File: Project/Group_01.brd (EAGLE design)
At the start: 71.1 x 54.3 mm, 29 parts, among them J1 POWER_JACKPTH_LOCK, U1 +12v, U4 TMUX1208

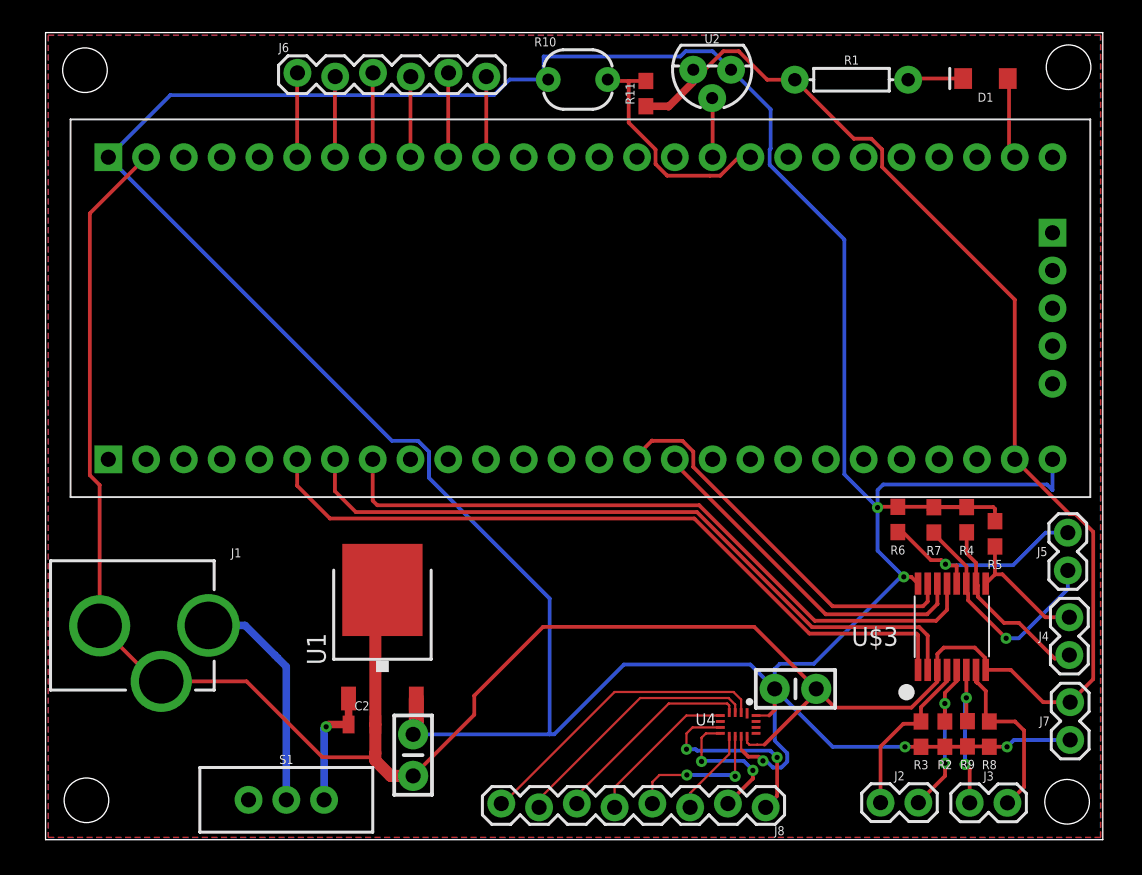
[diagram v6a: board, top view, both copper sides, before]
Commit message: Added measure in board
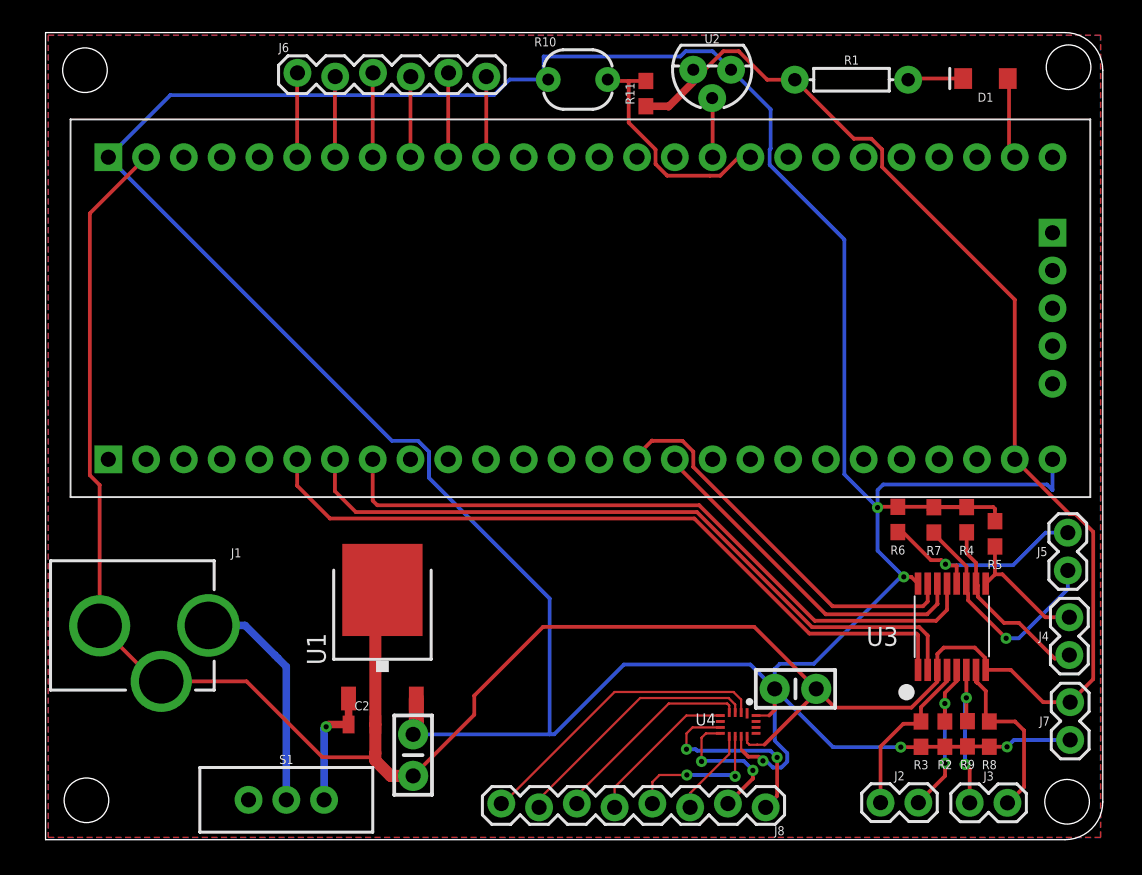
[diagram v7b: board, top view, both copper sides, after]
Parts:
- renumbered U$3 to U3
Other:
- outline, holes or cut-outs redrawn
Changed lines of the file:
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@@
 <setting verticaltext="up"/>
 </settings>
-<grid distance="0.1" unitdist="mil" unit="mil" style="lines" multiple="1" display="yes" altdistance="0.005" altunitdist="inch" altunit="inch"/>
+<grid distance="0.05" unitdist="inch" unit="inch" style="lines" multiple="1" display="yes" altdistance="0.005" altunitdist="inch" altunit="inch"/>
 <layers>
 <layer number="1" name="Top" color="4" fill="1" visible="yes" active="yes"/>
@@
 <layer number="23" name="tOrigins" color="15" fill="1" visible="yes" active="yes"/>
 <layer number="24" name="bOrigins" color="15" fill="1" visible="yes" active="yes"/>
-<layer number="25" name="tNames" color="7" fill="1" visible="yes" active="yes"/>
+<layer number="25" name="tNames" color="7" fill="1" visible="no" active="yes"/>
 <layer number="26" name="bNames" color="7" fill="1" visible="no" active="yes"/>
-<layer number="27" name="tValues" color="7" fill="1" visible="yes" active="yes"/>
+<layer number="27" name="tValues" color="7" fill="1" visible="no" active="yes"/>
 <layer number="28" name="bValues" color="7" fill="1" visible="no" active="yes"/>
 <layer number="29" name="tStop" color="7" fill="3" visible="no" active="yes"/>
 <layer number="30" name="bStop" color="7" fill="6" visible="no" active="yes"/>
-<layer number="31" name="tCream" color="7" fill="4" visible="no" active="yes"/>
+<layer number="31" name="tCream" color="7" fill="4" visible="yes" active="yes"/>
 <layer number="32" name="bCream" color="7" fill="5" visible="no" active="yes"/>
 <layer number="33" name="tFinish" color="6" fill="3" visible="no" active="yes"/>
@@
 <board>
 <plain>
-<wire x1="0" y1="0" x2="71.1" y2="0" width="0" layer="20"/>
-<wire x1="71.1" y1="0" x2="71.1" y2="54.28" width="0" layer="20"/>
-<wire x1="71.1" y1="54.28" x2="0" y2="54.28" width="0" layer="20"/>
 <wire x1="0" y1="54.28" x2="0" y2="0" width="0" layer="20"/>
+<wire x1="0" y1="0" x2="68.56" y2="0" width="0" layer="20"/>
+<wire x1="68.56" y1="0" x2="71.1" y2="2.54" width="0" layer="20" curve="90"/>
+<wire x1="71.1" y1="2.54" x2="71.1" y2="51.74" width="0" layer="20"/>
+<wire x1="71.1" y1="51.74" x2="68.56" y2="54.28" width="0" layer="20" curve="90"/>
+<wire x1="68.56" y1="54.28" x2="0" y2="54.28" width="0" layer="20"/>
 <hole x="2.65" y="51.75" drill="3"/>
 <hole x="68.8" y="51.95" drill="3"/>
 <hole x="2.75" y="2.65" drill="3"/>
 <hole x="68.7" y="2.55" drill="3"/>
+<dimension x1="0" y1="54.28" x2="0" y2="0" x3="-8.89" y3="27.14" textsize="1.778" textratio="15" layer="21" dtype="vertical"/>
+<dimension x1="0" y1="0" x2="71.12" y2="0" x3="35.56" y3="-15.24" textsize="1.778" textratio="15" layer="21" dtype="horizontal"/>
 </plain>
 <attributes>
@@
 <attribute name="VALUE" x="41.13478125" y="50.174271875" size="0.6096" layer="27" font="vector" ratio="20" rot="R90" align="top-center"/>
 </element>
-<element name="U$3" library="Group_01_Library" package="TSSOP16" value="TCA9546A" x="60.95" y="14.32" smashed="yes" rot="R90">
+<element name="U3" library="Group_01_Library" package="TSSOP16" value="TCA9546A" x="60.95" y="14.32" smashed="yes" rot="R90">
 <attribute name="NAME" x="57.347734375" y="13.668865625" size="1.27" layer="25" align="center-right"/>
 </element>
@@
 <contactref element="C1" pad="2"/>
 <contactref element="U1" pad="3"/>
-<contactref element="U$3" pad="8"/>
-<contactref element="U$3" pad="3"/>
+<contactref element="U3" pad="8"/>
+<contactref element="U3" pad="3"/>
 <contactref element="U$2" pad="28"/>
 <contactref element="R1" pad="P$1"/>
@@
 <contactref element="U1" pad="2"/>
 <contactref element="C1" pad="1"/>
-<contactref element="U$3" pad="16"/>
+<contactref element="U3" pad="16"/>
 <contactref element="R2" pad="2"/>
 <contactref element="R3" pad="2"/>
@@
 <wire x1="38.89501875" y1="11.78051875" x2="47.397321875" y2="11.78051875" width="0.254" layer="16"/>
 <wire x1="47.397321875" y1="11.78051875" x2="49.035459375" y2="10.14238125" width="0.254" layer="16"/>
-<wire x1="57.79945" y1="6.247609375" x2="57.7977" y2="6.245859375" width="0.254" layer="1"/>
-<via x="57.7977" y="6.245859375" extent="1-16" drill="0.35"/>
-<wire x1="57.7977" y1="6.245859375" x2="52.93198125" y2="6.245859375" width="0.254" layer="16"/>
-<wire x1="52.93198125" y1="6.245859375" x2="49.035459375" y2="10.14238125" width="0.254" layer="16"/>
+<wire x1="57.5175125" y1="6.2272875" x2="57.5157625" y2="6.2255375" width="0.254" layer="1"/>
+<via x="57.5157625" y="6.2255375" extent="1-16" drill="0.35"/>
+<wire x1="57.5157625" y1="6.2255375" x2="52.952303125" y2="6.2255375" width="0.254" layer="16"/>
+<wire x1="52.952303125" y1="6.2255375" x2="49.035459375" y2="10.14238125" width="0.254" layer="16"/>
 <wire x1="60.48" y1="6.25" x2="61.98" y2="6.25" width="0.254" layer="1"/>
 <wire x1="61.98" y1="6.25" x2="62" y2="6.27" width="0.254" layer="1"/>
@@
 <vertex x="0.187959375" y="0.180340625"/>
 </polygon>
-<wire x1="57.7977" y1="6.245859375" x2="58.872540625" y2="6.245859375" width="0.254" layer="1"/>
-<wire x1="58.872540625" y1="6.245859375" x2="58.874290625" y2="6.247609375" width="0.254" layer="1"/>
+<wire x1="57.5157625" y1="6.2255375" x2="58.85221875" y2="6.2255375" width="0.254" layer="1"/>
+<wire x1="58.85221875" y1="6.2255375" x2="58.874290625" y2="6.247609375" width="0.254" layer="1"/>
 <wire x1="58.874290625" y1="6.247609375" x2="60.477609375" y2="6.247609375" width="0.254" layer="1"/>
 <wire x1="60.477609375" y1="6.247609375" x2="60.48" y2="6.25" width="0.254" layer="1"/>
@@
 </signal>
 <signal name="I2C_SCL_0">
-<contactref element="U$3" pad="5"/>
+<contactref element="U3" pad="5"/>
 <contactref element="R2" pad="1"/>
 <contactref element="J2" pad="2"/>
@@
 <signal name="I2C_SDA_0">
 <contactref element="R3" pad="1"/>
-<contactref element="U$3" pad="4"/>
+<contactref element="U3" pad="4"/>
 <contactref element="J2" pad="1"/>
 <wire x1="60.625" y1="11.42" x2="60.625" y2="10.66395" width="0.254" layer="1"/>
@@
 </signal>
 <signal name="I2C_SDA_1">
-<contactref element="U$3" pad="6"/>
+<contactref element="U3" pad="6"/>
 <contactref element="R9" pad="1"/>
 <contactref element="J3" pad="1"/>
@@
 <signal name="I2C_SCL_1">
 <contactref element="R8" pad="1"/>
-<contactref element="U$3" pad="7"/>
+<contactref element="U3" pad="7"/>
 <contactref element="J3" pad="2"/>
 <wire x1="63.47" y1="7.95" x2="63.2333" y2="8.1867" width="0.254" layer="1"/>
@@
 </signal>
 <signal name="I2C_SDA_2">
-<contactref element="U$3" pad="9"/>
+<contactref element="U3" pad="9"/>
 <contactref element="R5" pad="1"/>
 <contactref element="J4" pad="1"/>
@@
 <signal name="I2C_SCL_2">
 <contactref element="R4" pad="1"/>
-<contactref element="U$3" pad="10"/>
+<contactref element="U3" pad="10"/>
 <contactref element="J4" pad="2"/>
 <wire x1="61.946959375" y1="20.669490625" x2="61.946959375" y2="19.24795" width="0.254" layer="1"/>
@@
 </signal>
 <signal name="I2C_SCL_3">
-<contactref element="U$3" pad="12"/>
+<contactref element="U3" pad="12"/>
 <contactref element="R6" pad="1"/>
 <contactref element="J5" pad="2"/>
@@
 </signal>
 <signal name="I2C_SDA_3">
-<contactref element="U$3" pad="11"/>
+<contactref element="U3" pad="11"/>
 <contactref element="R7" pad="1"/>
 <contactref element="J5" pad="1"/>
@@
 </signal>
 <signal name="I2C_SDA">
-<contactref element="U$3" pad="15"/>
+<contactref element="U3" pad="15"/>
 <contactref element="U$2" pad="15"/>
 <wire x1="43.5628" y1="26.0947875" x2="42.8347875" y2="26.8228" width="0.254" layer="1"/>
@@
 </signal>
 <signal name="I2C_SCL">
-<contactref element="U$3" pad="14"/>
+<contactref element="U3" pad="14"/>
 <contactref element="U$2" pad="16"/>
 <wire x1="59.975" y1="17.22" x2="59.975" y2="15.866859375" width="0.254" layer="1"/>
@@
 </signal>
 <signal name="I2C_A2">
-<contactref element="U$3" pad="13"/>
+<contactref element="U3" pad="13"/>
 <contactref element="U$2" pad="8"/>
 <wire x1="60.625" y1="17.22" x2="60.625" y2="15.45490625" width="0.254" layer="1"/>
@@
 </signal>
 <signal name="I2C_A1">
-<contactref element="U$3" pad="2"/>
+<contactref element="U3" pad="2"/>
 <contactref element="U$2" pad="7"/>
 <wire x1="59.325" y1="11.42" x2="59.325" y2="13.730478125" width="0.254" layer="1"/>
@@
 </signal>
 <signal name="I2C_A0">
-<contactref element="U$3" pad="1"/>
+<contactref element="U3" pad="1"/>
 <contactref element="U$2" pad="6"/>
 <wire x1="58.675" y1="11.42" x2="58.675" y2="13.76981875" width="0.254" layer="1"/>
@@
 <contactref element="U$2" pad="51"/>
 <contactref element="D1" pad="A"/>
-<wire x1="64.71" y1="51.19" x2="64.79391875" y2="51.10608125" width="0.254" layer="1"/>
-<wire x1="64.79391875" y1="51.10608125" x2="64.79391875" y2="46.28608125" width="0.254" layer="1"/>
+<wire x1="64.71" y1="51.19" x2="64.79391875" y2="50.987403125" width="0.254" layer="1" curve="-45"/>
+<wire x1="64.79391875" y1="50.987403125" x2="64.79391875" y2="46.28608125" width="0.254" layer="1"/>
 <wire x1="64.79391875" y1="46.28608125" x2="65.18" y2="45.9" width="0.254" layer="1"/>
 </signal>

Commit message: Fixed connection between mux and microcontroller
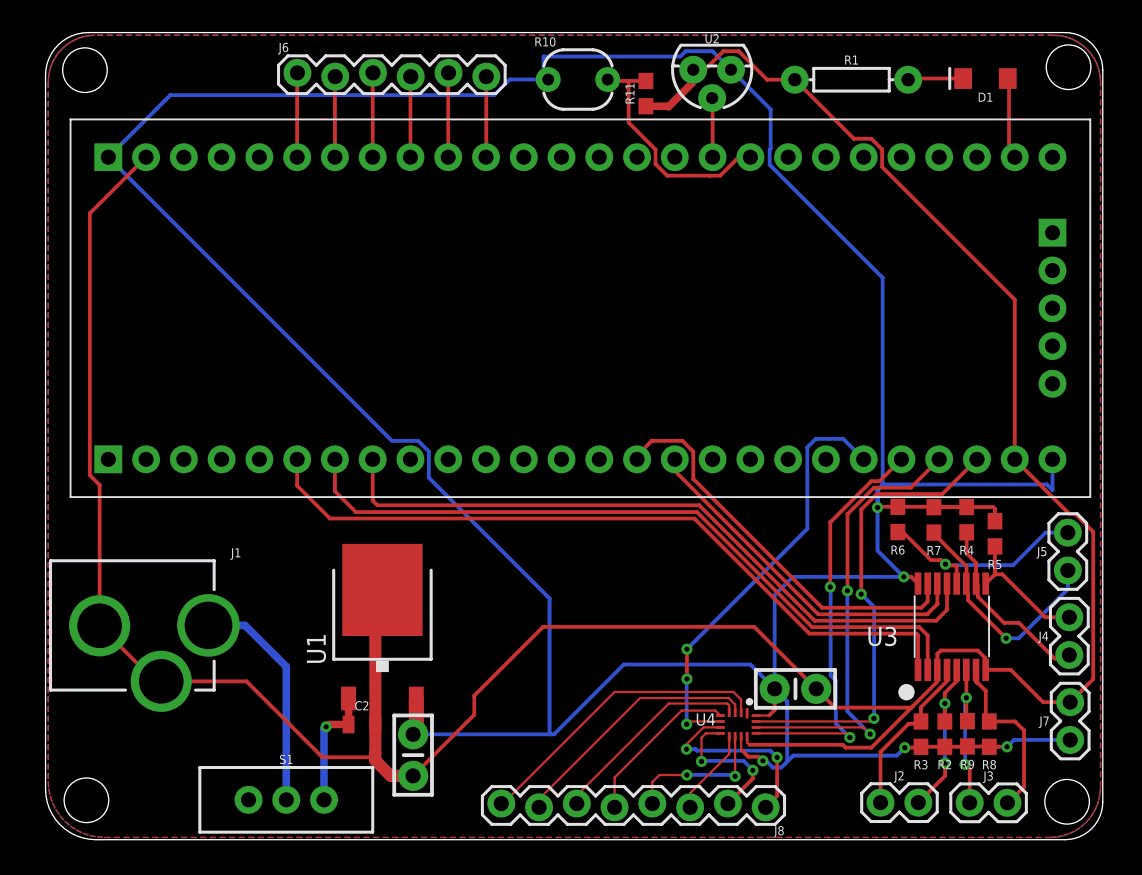
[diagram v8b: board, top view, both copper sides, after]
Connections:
- removed net MUX_A0/1.3C: U4.15
- removed net MUX_A0/2.3C: U$2.24
- removed net MUX_A1/1.4C: U4.14
- removed net MUX_A1/2.3C: U$2.23
- removed net MUX_A2/1.4C: U4.13
- removed net MUX_A2/2.3C: U$2.22
- removed net MUX_OUT/1.4C: U4.6
- removed net MUX_OUT/2.5C: U$2.21
- new net MUX_A0: U$2.24, U4.15
- new net MUX_A1: U$2.23, U4.14
- new net MUX_A2: U$2.22, U4.13
- new net MUX_OUT: U$2.21, U4.6
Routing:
- net MUX_A0: track 0.00 -> 31.6 mm, vias 0 -> 2
- net MUX_A1: track 0.00 -> 31.0 mm, vias 0 -> 2
- net MUX_OUT: track 0.00 -> 28.9 mm, vias 0 -> 3
- net MUX_A2: track 0.00 -> 28.0 mm, vias 0 -> 2
- net GND: track 198.0 -> 203.6 mm
- net 5V: track 242.8 -> 243.9 mm
- net N$13: track 10.5 -> 11.1 mm
- net I2C_SDA: track 26.8 -> 27.3 mm
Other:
- outline, holes or cut-outs redrawn
